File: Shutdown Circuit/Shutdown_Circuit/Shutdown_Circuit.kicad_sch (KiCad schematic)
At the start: 21 parts, among them J2 776280-1, K1 V23047A1012A511, K2 V23047A1012A511, K3 V23047A1012A511, Q1 2N2222, Q2 2N2222, Q3 2N2222

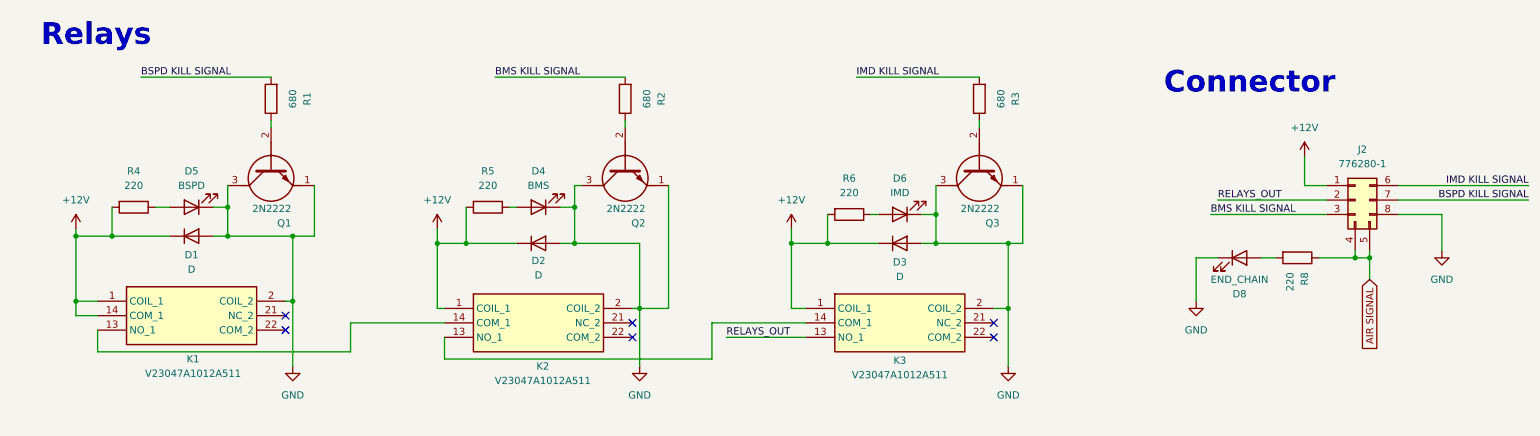
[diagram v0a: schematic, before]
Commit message: BSPD, Shutdown/Charging Shutdown, & Voltage Indicator final changes
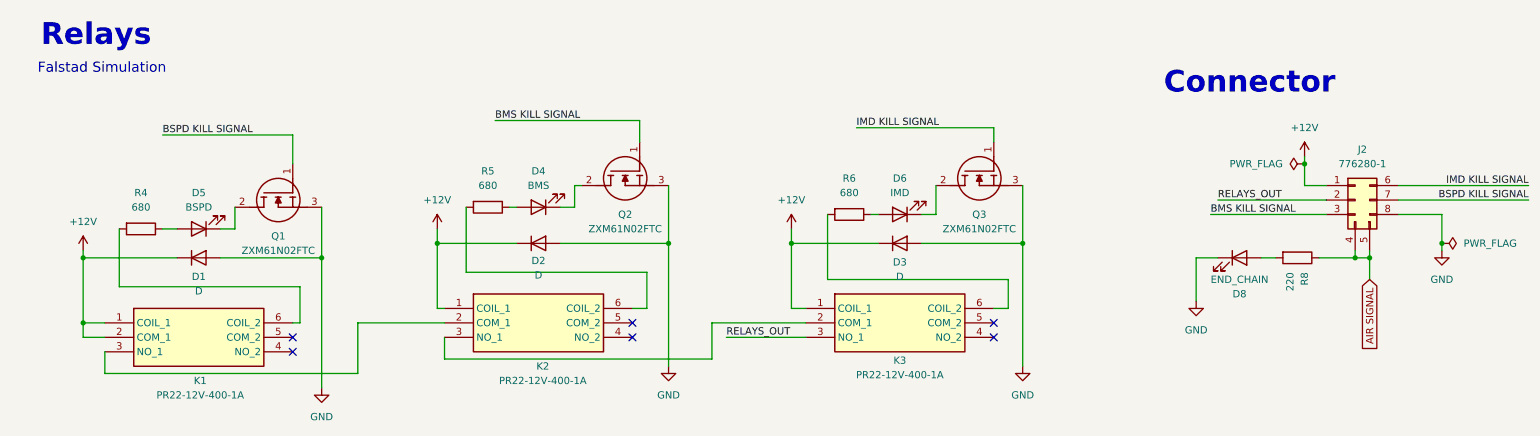
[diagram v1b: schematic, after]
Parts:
- removed Q1, Q2, Q3: 2N2222, Package_TO_SOT_THT:2N2222, symbol Transistor_BJT:2N2222
- removed R1, R2, R3: 680, Resistor_SMD:R_0603_1608Metric, symbol Device:R
- added Q1, Q2, Q3: ZXM61N02FTC, Misc_footprints:ZXM61N02FTC, symbol V23047A1012A511:ZXM61N02FTC
- K1, K2, K3: value V23047A1012A511 -> PR22-12V-400-1A; footprint Misc_footprints:V23047A1012A511 -> Misc_footprints:PR2212V4001A; symbol V23047A1012A511:V23047A1012A511 -> V23047A1012A511:PR22-12V-400-1A; Height 25.5 -> 16.1; Manufacturer_Name TE Connectivity -> Same Sky; Manufacturer_Part_Number V23047A1012A511 -> PR22-12V-400-1A
- R4, R5, R6: value 220 -> 680
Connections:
- net +12V: now also K1.2 (COM_1); no longer K1.14 (COM_1), R4.2, R5.2, R6.2
- net BMS KILL SIGNAL: now also Q2.1 (G)
- net BSPD KILL SIGNAL: now also Q1.1 (G)
- net GND: now also Q1.3 (S), Q2.3 (S), Q3.3 (S); no longer D4.1 (K), D5.1 (K), D6.1 (K), K1.2 (COIL_2), K2.2 (COIL_2), K3.2 (COIL_2)
- net IMD KILL SIGNAL: now also Q3.1 (G)
- net RELAYS_OUT: now also K3.3 (NO_1); no longer K3.13 (NO_1)
- new net: D6.1 (K), Q3.2 (D)
- new net: D5.1 (K), Q1.2 (D)
- new net: D4.1 (K), Q2.2 (D)
- new net: K2.6 (COIL_2), R5.2
- new net: K1.6 (COIL_2), R4.2
- new net: K1.3 (NO_1), K2.2 (COM_1)
- new net: K2.3 (NO_1), K3.2 (COM_1)
- new net: K3.6 (COIL_2), R6.2
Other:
- note added: "Falstad Simulation"
- moved on the sheet: D1, D5, K1, R4
